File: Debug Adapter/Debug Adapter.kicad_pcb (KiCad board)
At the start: 2 copper layers, 17.8 x 25.3 mm, 8 parts, among them J1 Conn_01x03_Pin, J2 Conn_01x06_Pin, J3 Conn_01x06_Socket, U1 VOD207T

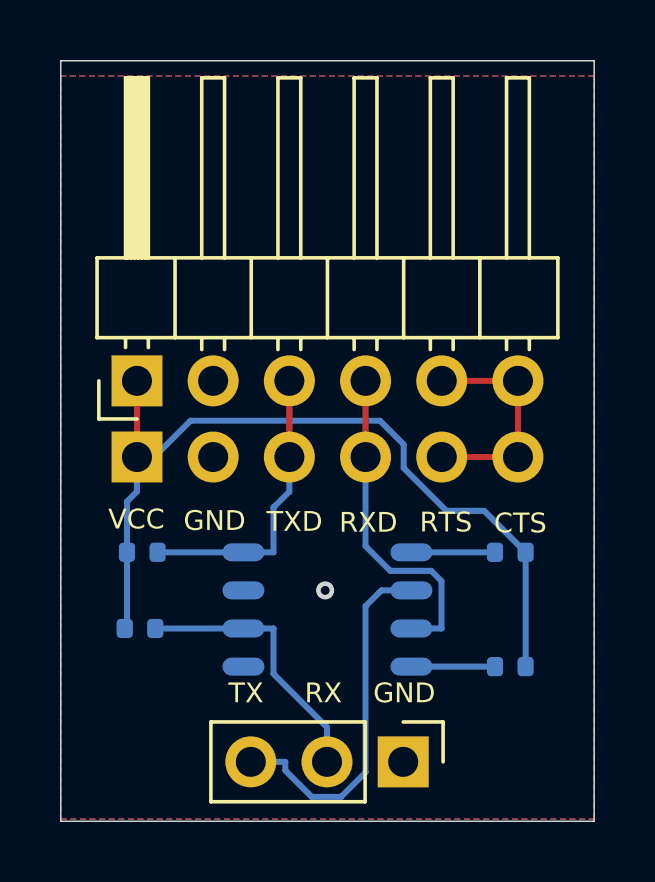
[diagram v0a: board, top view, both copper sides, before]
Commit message: More temperature adjustments
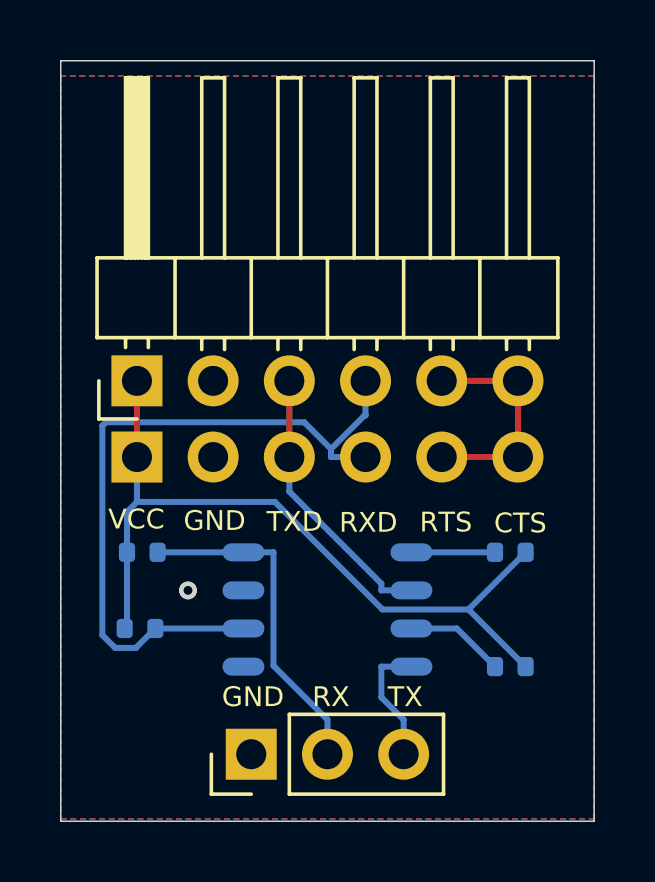
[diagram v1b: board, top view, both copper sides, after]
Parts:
- moved J1 5.07 mm to (138.4, 88.6), turned to 90 degrees
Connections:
- J1 pad 2: RXD MCU -> RXD Reflow
- J1 pad 3: TXD MCU -> TXD Reflow
- R3 pad 1: RXD MCU -> RXD
- R4 pad 1: TXD -> RXD Reflow
- U1 pad 2: TXD MCU -> TXD
- U1 pad 3: RXD -> Net-(R2-Pad2)
- U1 pad 4: Net-(R2-Pad2) -> TXD Reflow
- U1 pad 6: RXD MCU -> RXD
- U1 pad 8: TXD -> RXD Reflow
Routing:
- net RXD: track 11.1 -> 24.4 mm
- net TXD MCU: track 12.1 -> 0.00 mm
- net RXD Reflow: track 0.00 -> 11.3 mm
- net RXD MCU: track 9.12 -> 0.00 mm
- net TXD Reflow: track 0.00 -> 4.23 mm
- net +5V: track 28.2 -> 26.3 mm
- net TXD: track 9.80 -> 9.26 mm
- net Net-(R2-Pad2): track 2.79 -> 3.31 mm
